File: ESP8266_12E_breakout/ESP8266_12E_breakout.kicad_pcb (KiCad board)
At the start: 2 copper layers, 10 parts, among them J2 CONN_01X08, J3 CONN_01X08, U1 ESP-12E

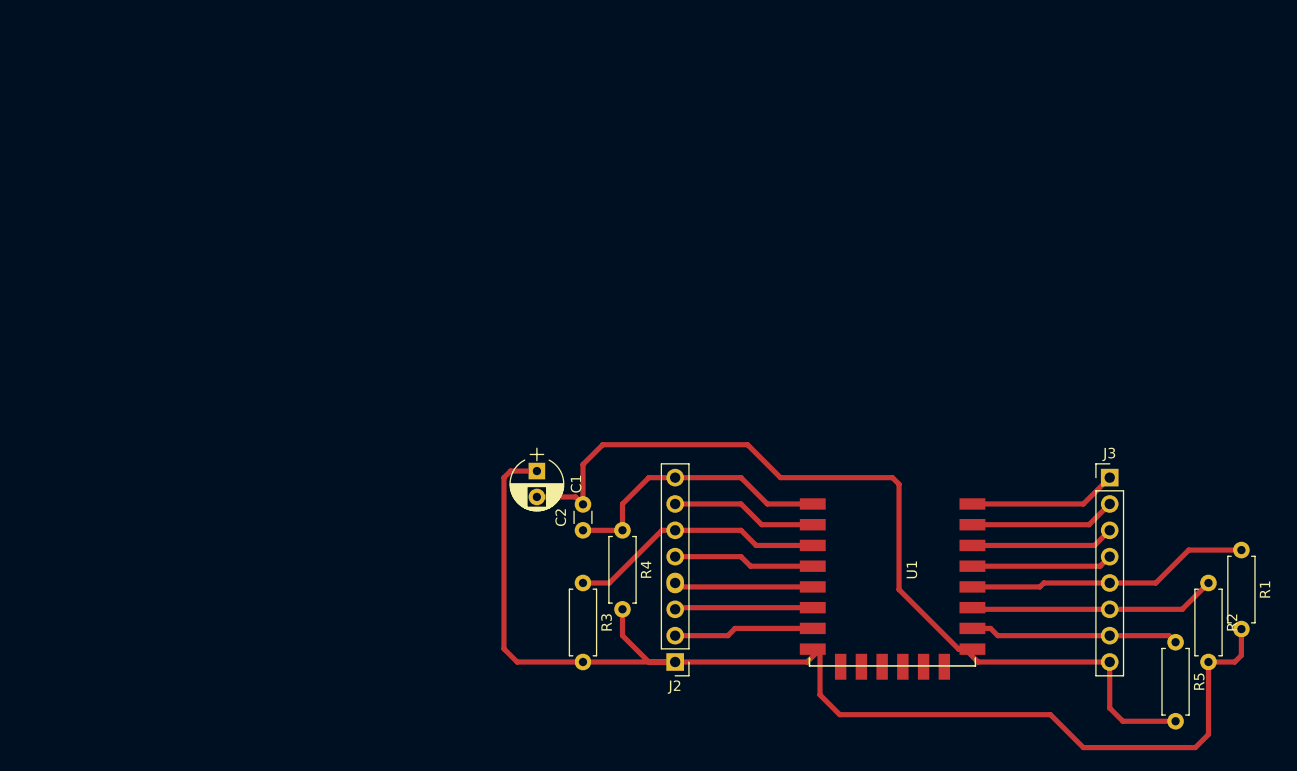
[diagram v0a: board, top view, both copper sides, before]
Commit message: pushed pad size to accomodate more solder area
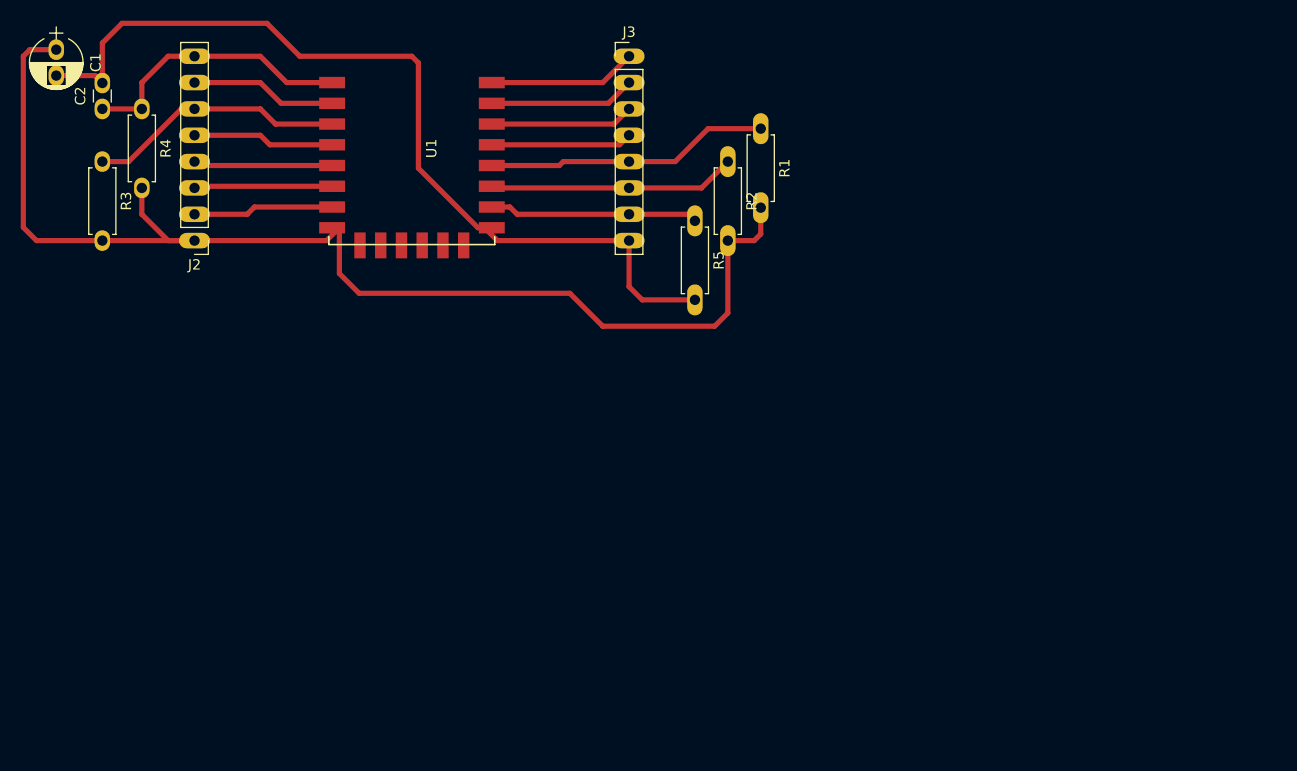
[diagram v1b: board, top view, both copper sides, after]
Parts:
- moved C1 61.6 mm to (27.9, 27.3)
- moved J2 61.6 mm to (41.3, 45.7)
- moved R1 61.6 mm to (95.9, 34.9)
- moved R2 61.6 mm to (92.7, 38.1)
- moved U1 61.6 mm to (55.2, 30.5)
- moved C2 61.6 mm to (32.4, 33.0)
- moved J3 61.6 mm to (83.2, 27.9)
- moved R3 61.6 mm to (32.4, 38.1)
- moved R4 61.6 mm to (36.2, 33.0)
- moved R5 61.6 mm to (89.5, 43.8)
